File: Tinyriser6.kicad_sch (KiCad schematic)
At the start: 22 parts, among them J2 Bus_PCI_Express_x16, J3 Bus_M.2_Socket_M, J4 Conn_02x04_Odd_Even, J5 USB_A, J6 Conn_02x10_Top_Bottom, J8 Conn_02x10_Odd_Even, M1 Fan_4pin

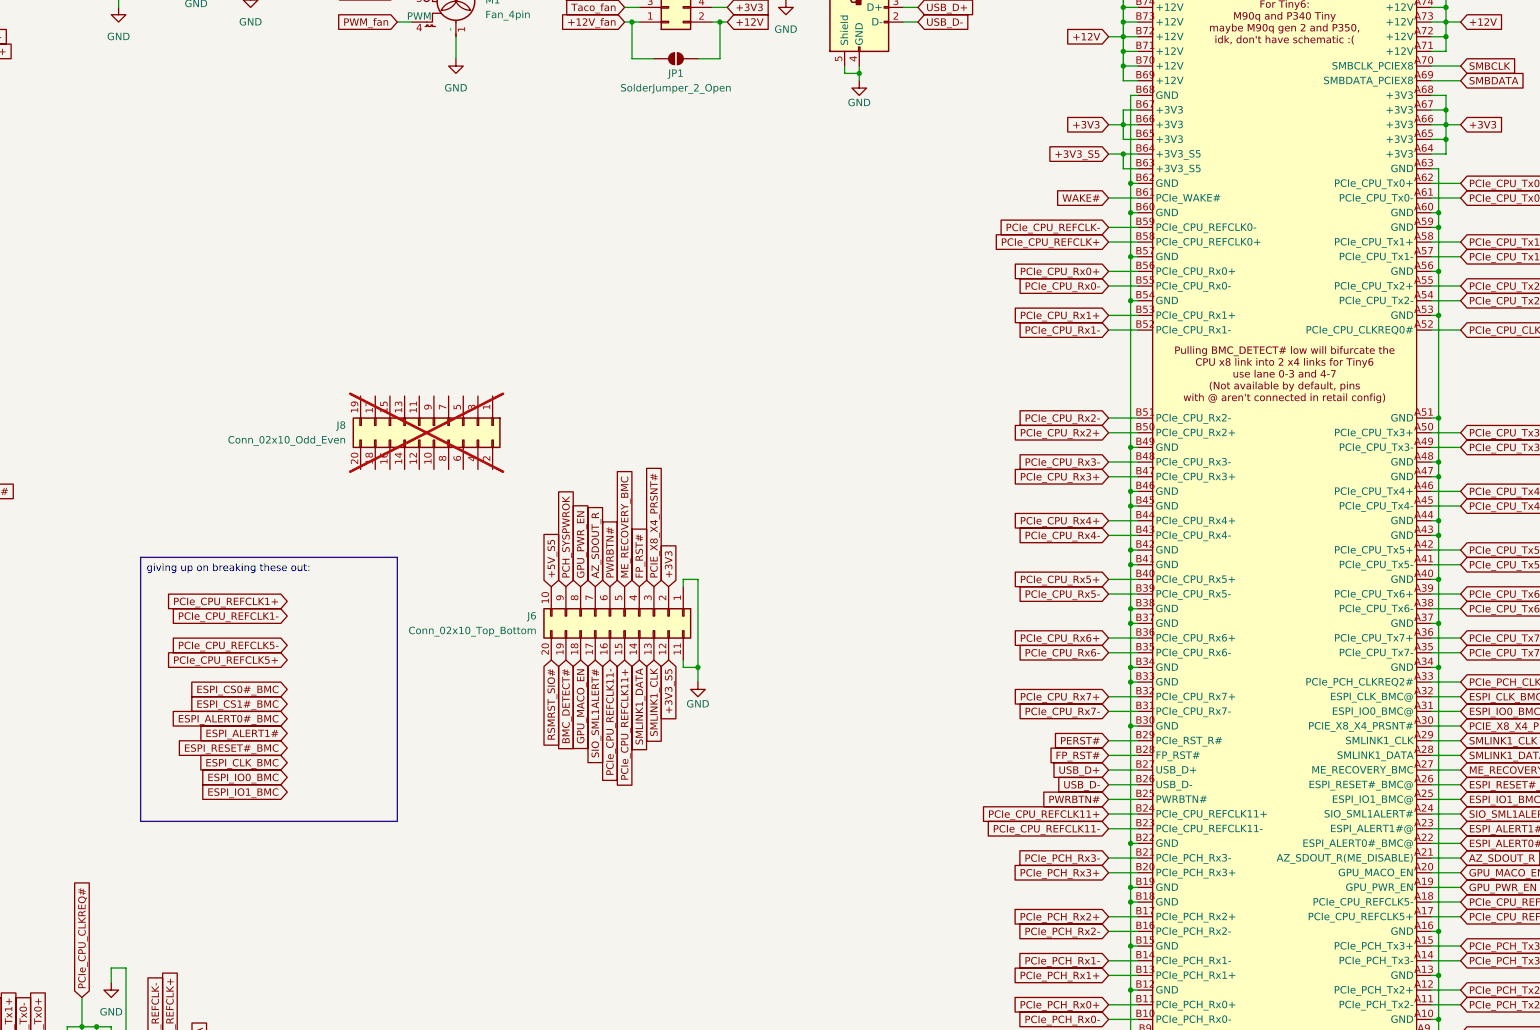
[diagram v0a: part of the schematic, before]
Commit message: Slight copper fill optimizations
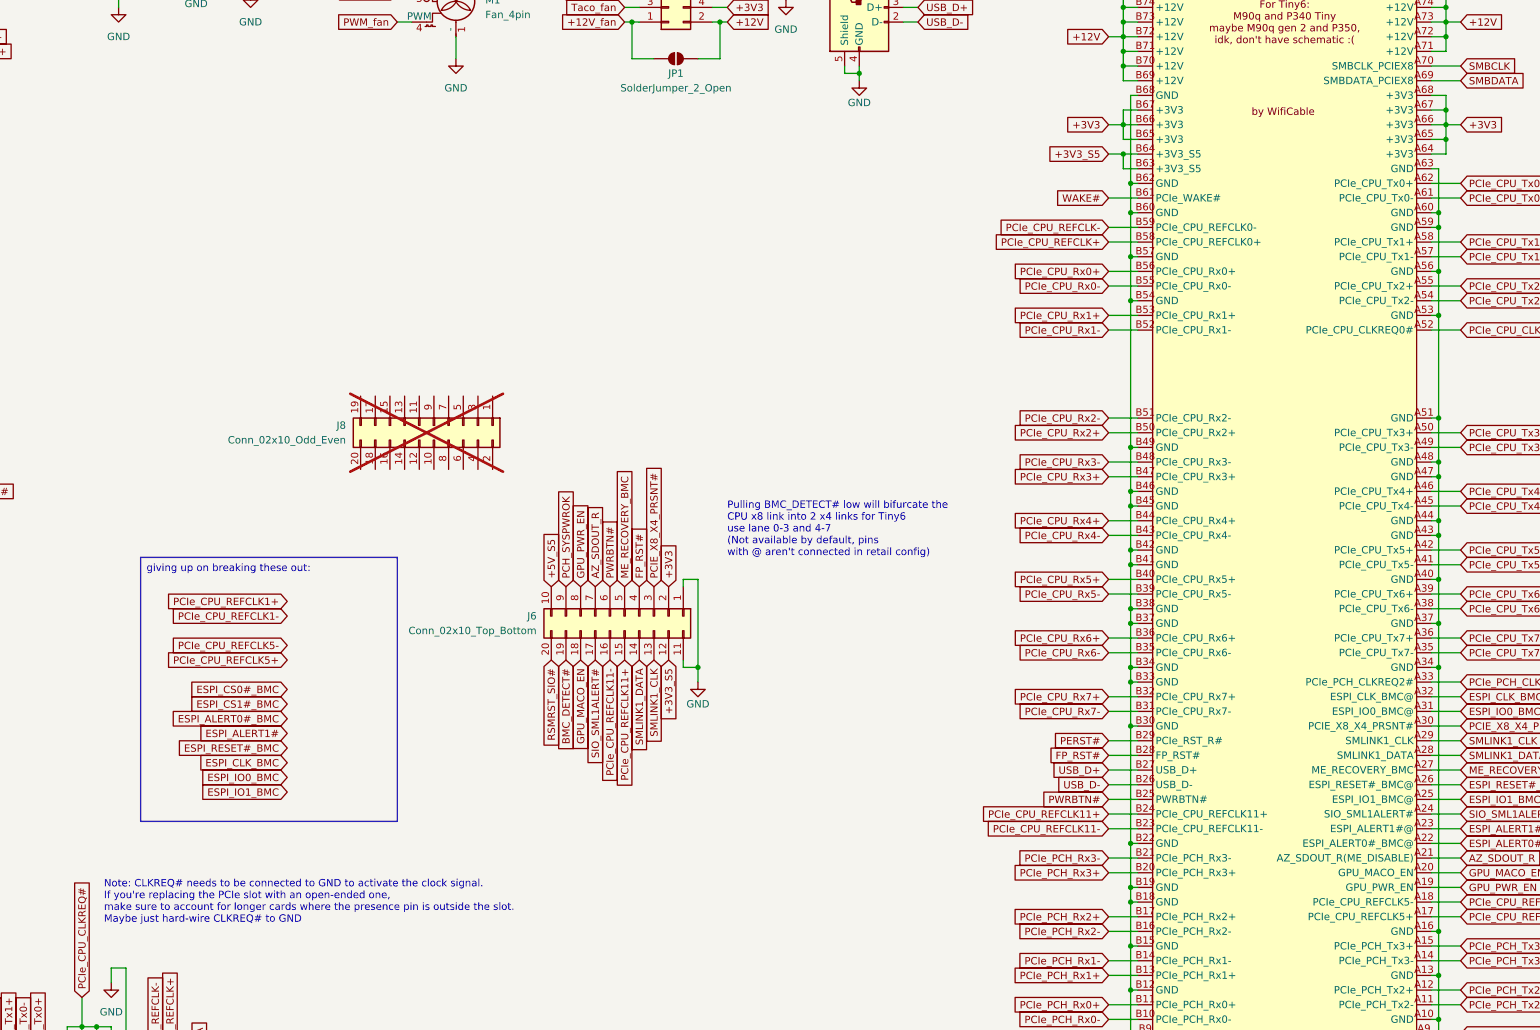
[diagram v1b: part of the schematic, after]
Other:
- note added: "Note: CLKREQ# needs to be connected to GND to activate the clock signal. If you're replacing the PCIe slot with an open-ended one, make sure to account for longer cards where the presence pin is outside the slot. Maybe just hard-wire CLKREQ# to GND"
- note added: "Pulling BMC_DETECT# low will bifurcate the CPU x8 link into 2 x4 links for Tiny6 use lane 0-3 and 4-7 (Not available by default, pins with @ aren't connected in retail config)"

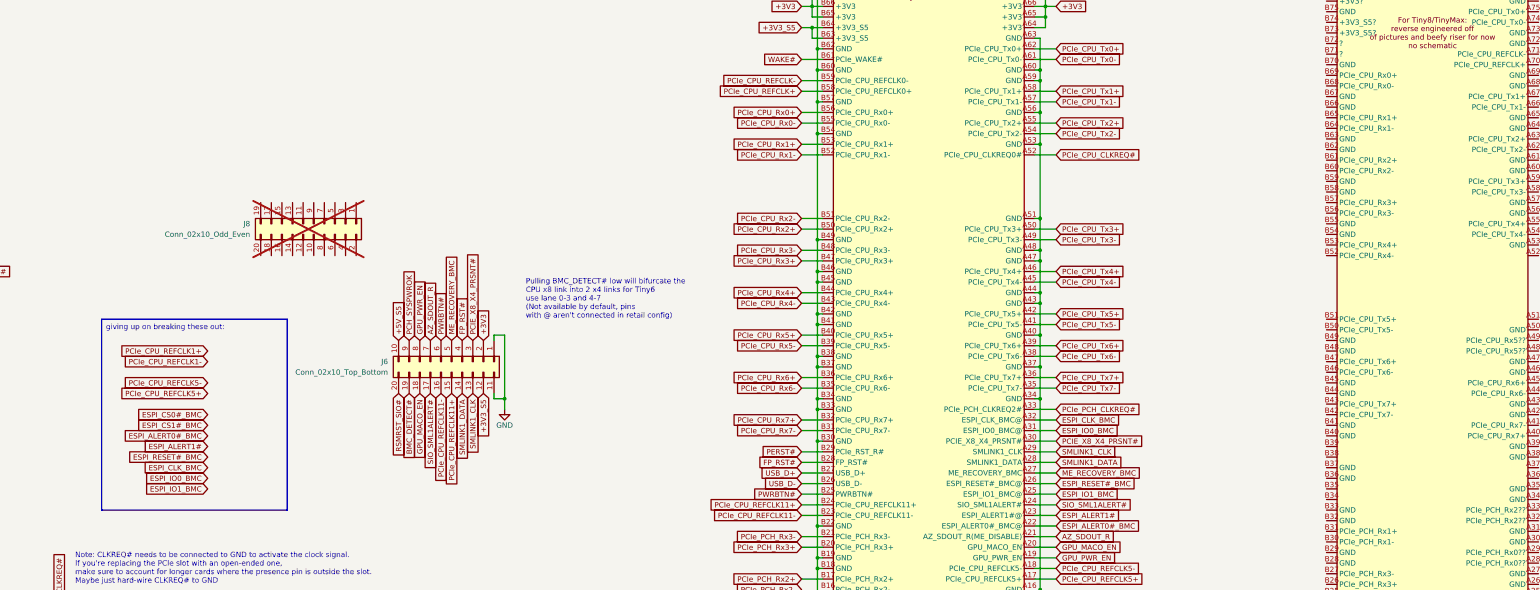
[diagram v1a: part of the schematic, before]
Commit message: Some schematic notes
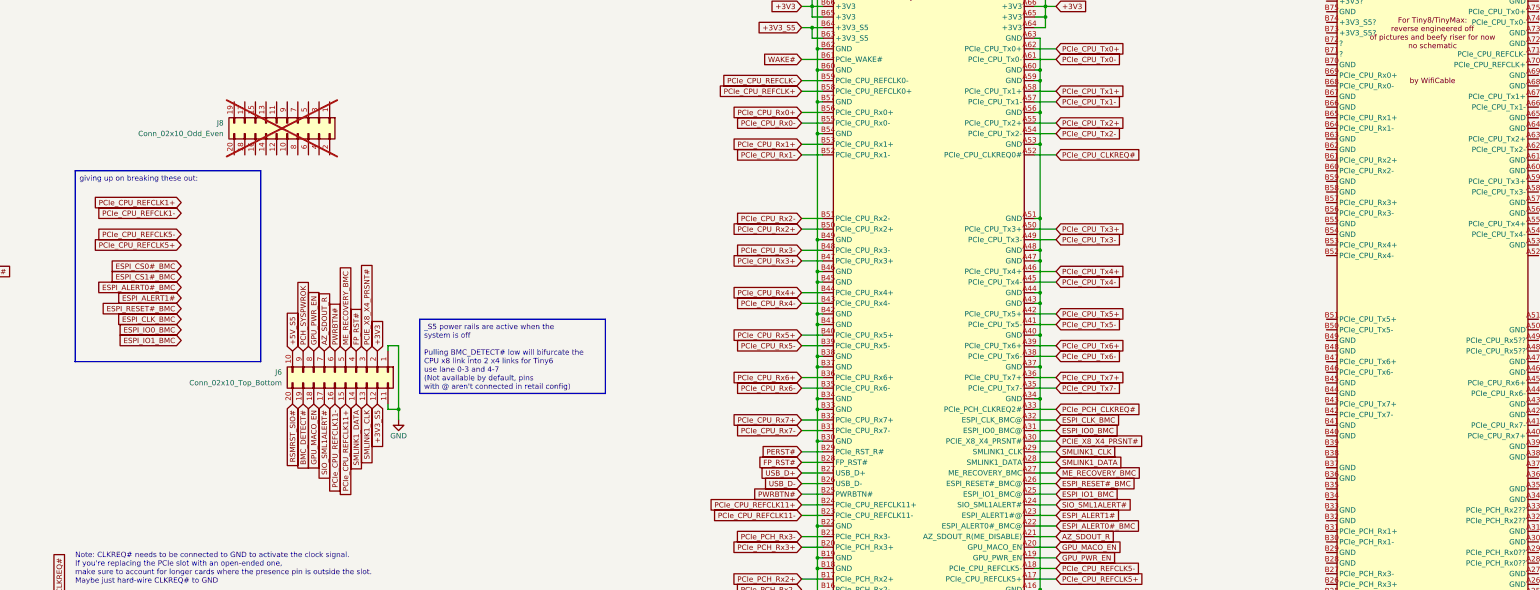
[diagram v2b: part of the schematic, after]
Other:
- note removed: "Pulling BMC_DETECT# low will bifurcate the CPU x8 link into 2 x4 links for Tiny6 use lane 0-3 and 4-7 (Not available by default, pins with @ aren't connected in retail config)"
- moved on the sheet: J6, J8

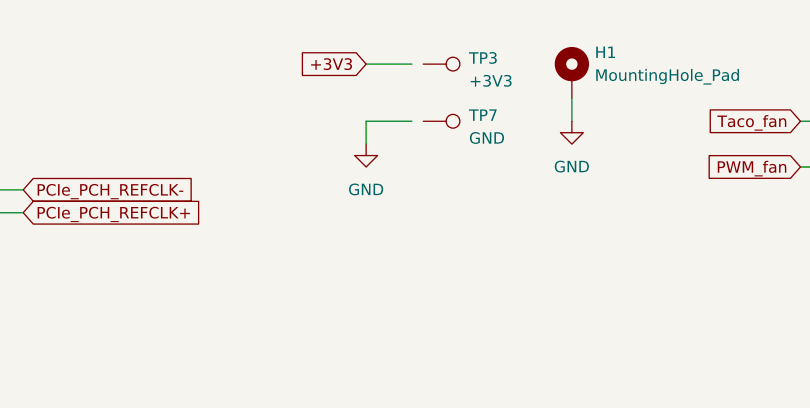
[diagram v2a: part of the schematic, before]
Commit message: removed some leftovers
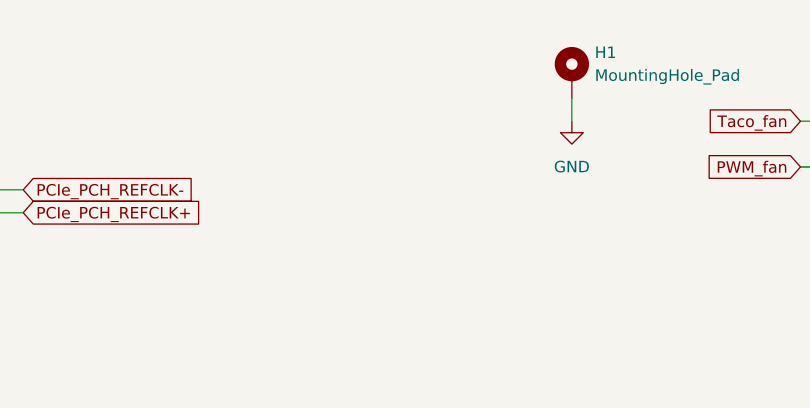
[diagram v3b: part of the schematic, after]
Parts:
- removed TP3: +3V3, TestPoint:TestPoint_THTPad_D1.5mm_Drill0.7mm, symbol Connector:TestPoint
- removed TP7: GND, TestPoint:TestPoint_THTPad_D1.5mm_Drill0.7mm, symbol Connector:TestPoint

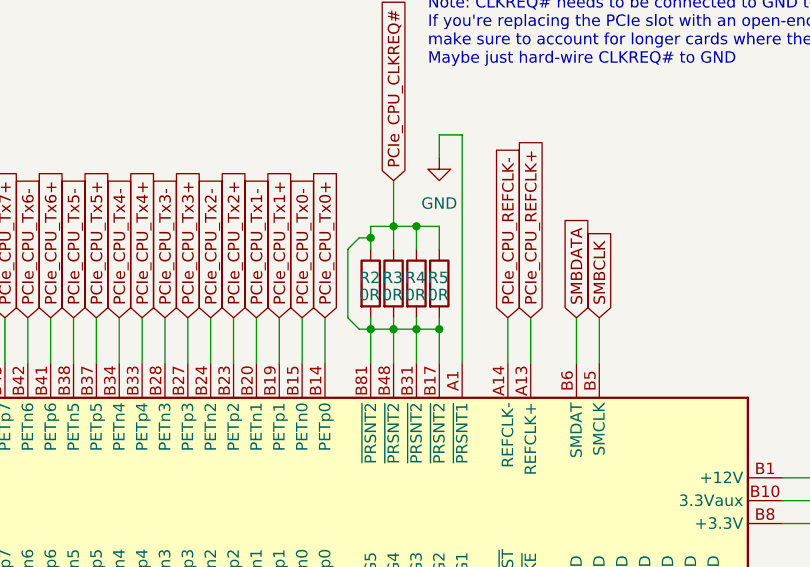
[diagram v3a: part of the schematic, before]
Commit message: Set clkreq resistors to DNP
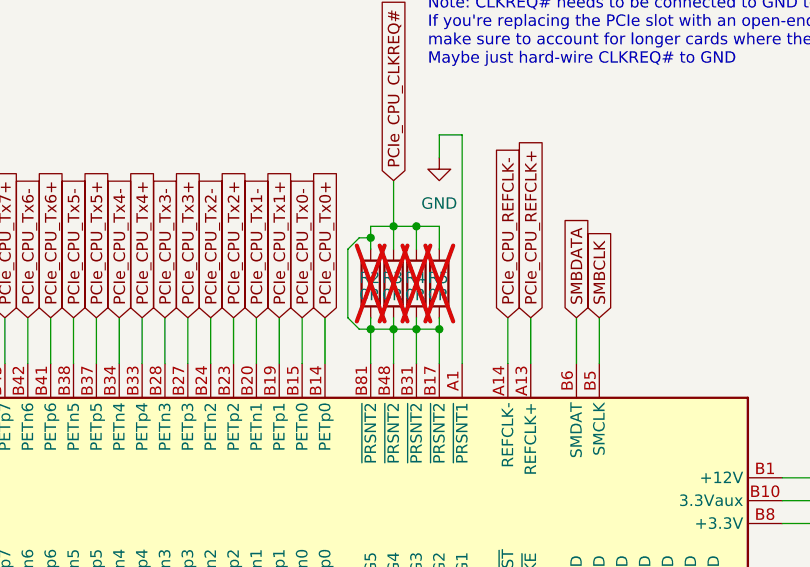
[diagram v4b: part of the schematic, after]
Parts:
- R2, R3, R4, R5: now not fitted
